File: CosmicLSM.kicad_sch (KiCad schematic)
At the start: 49 parts, among them J1 BAT, J2 JST GH, J3 USB_C_Receptacle_USB2.0, SW1 SW_SPDT, SW2 SW_SPST, U1 SMF05CT1G, U2 SMF05CT1G, U3 M3406, U4 IP2312, U5 LSM6DSV, U6 ESP32-C3-WROOM-02-N4

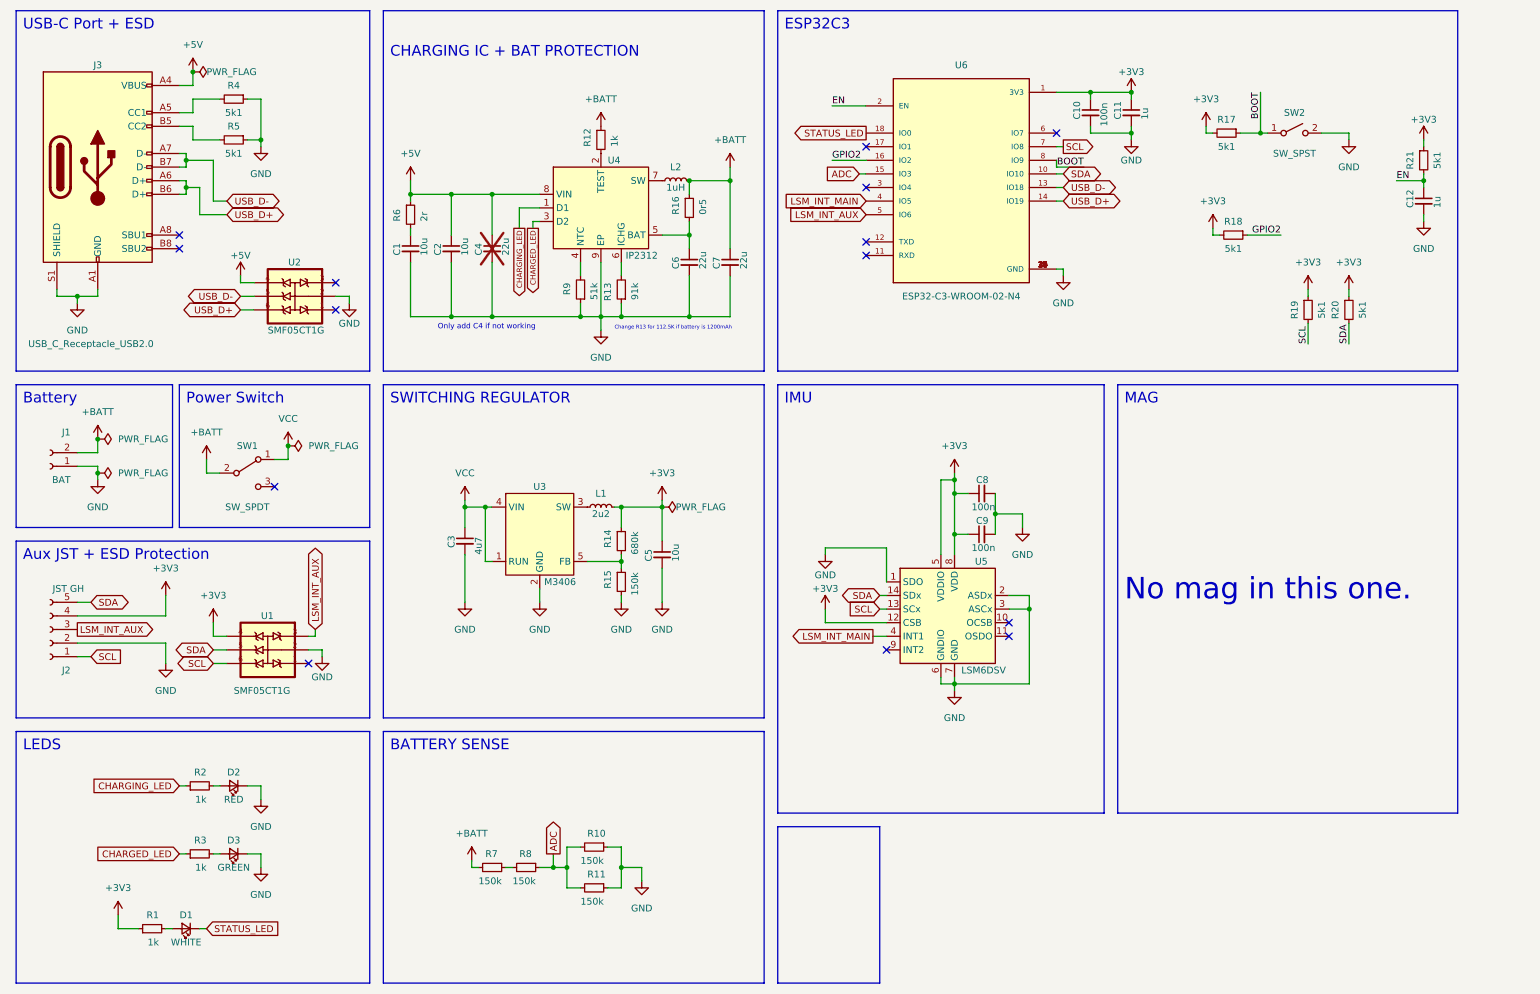
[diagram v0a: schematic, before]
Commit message: use ESP32-C6 in schematic
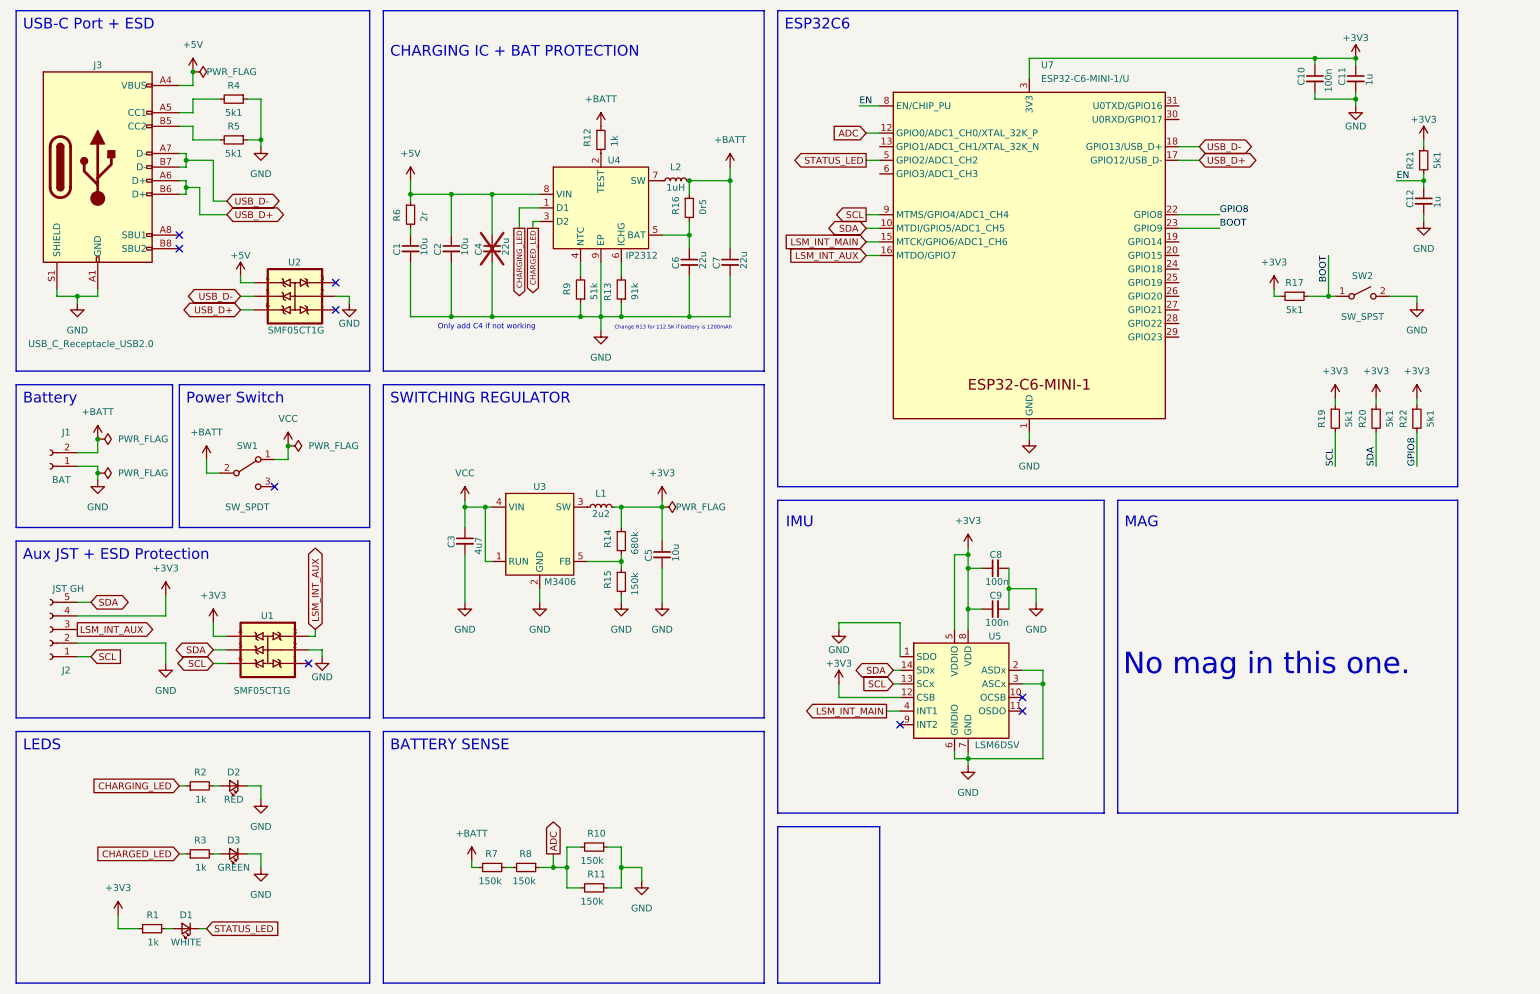
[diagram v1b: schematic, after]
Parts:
- removed R18: 5k1, Resistor_SMD:R_0603_1608Metric_Pad0.98x0.95mm_HandSolder, symbol CosmicLSM_Symbols:R_Small
- removed U6: ESP32-C3-WROOM-02-N4, footprints:MODULE_ESP32-C3-WROOM-02-H4, symbol CosmicLSM_Symbols:ESP32-C3-WROOM-02-N4
- added R22: 5k1, Resistor_SMD:R_0603_1608Metric_Pad0.98x0.95mm_HandSolder, symbol CosmicLSM_Symbols:R_Small
- added U7: ESP32-C6-MINI-1/U, Espressif:ESP32-C6-MINI-1, symbol Espressif:ESP32-C6-MINI-1/U
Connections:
- net +3V3: now also R22.1, U7.3 (3V3)
- net ADC: now also U7.12 (GPIO0/ADC1_CH0/XTAL_32K_P)
- net BOOT: now also U7.23 (GPIO9)
- net EN: now also U7.8 (EN/CHIP_PU)
- net GND: now also U7.1 (GND), U7.11 (GND), U7.14 (GND), U7.2 (GND), U7.36 (GND), U7.37 (GND), U7.38 (GND), U7.39 (GND), U7.40 (GND), U7.41 (GND), U7.42 (GND), U7.43 (GND), U7.44 (GND), U7.45 (GND), U7.46 (GND), U7.47 (GND), U7.48 (GND), U7.49 (GND), U7.50 (GND), U7.51 (GND), U7.52 (GND), U7.53 (GND)
- net LSM_INT_AUX: now also U7.16 (MTDO/GPIO7)
- net LSM_INT_MAIN: now also U7.15 (MTCK/GPIO6/ADC1_CH6)
- net SCL: now also U7.9 (MTMS/GPIO4/ADC1_CH4)
- net SDA: now also U7.10 (MTDI/GPIO5/ADC1_CH5)
- net STATUS_LED: now also U7.5 (GPIO2/ADC1_CH2)
- net USB_D+: now also U7.17 (GPIO12/USB_D-)
- net USB_D-: now also U7.18 (GPIO13/USB_D+)
- new net GPIO8: R22.2, U7.22 (GPIO8)
- no-connect marks 14 -> 9
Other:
- note added: "ESP32C6"
- note removed: "ESP32C3"
- moved on the sheet: C8, C9, R17, R19, R20, SW2, U5

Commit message: new data
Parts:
- U5: value LSM6DSV -> BMI160
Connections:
- net LSM_INT_MAIN: now also U7.26 (GPIO20); no longer U7.15 (MTCK/GPIO6/ADC1_CH6)
- net SCL: now also U7.28 (GPIO22); no longer U7.9 (MTMS/GPIO4/ADC1_CH4)
- net SDA: now also U7.27 (GPIO21); no longer U7.10 (MTDI/GPIO5/ADC1_CH5)
- net USB_D+: now also U2.5; no longer U2.6
- net USB_D-: now also U2.6; no longer U2.5
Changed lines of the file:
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@@
 	(wire
 		(pts
-			(xy 172.72 54.61) (xy 175.26 54.61)
-		)
-		(stroke
-			(width 0)
-			(type default)
-		)
-	)
-	(wire
-		(pts
 			(xy 73.66 67.31) (xy 76.2 67.31)
 		)
@@
 	(wire
 		(pts
-			(xy 45.72 41.91) (xy 45.72 40.64)
+			(xy 231.14 67.31) (xy 236.22 67.31)
 		)
 		(stroke
@@
 	(wire
 		(pts
-			(xy 172.72 57.15) (xy 175.26 57.15)
+			(xy 231.14 72.39) (xy 236.22 72.39)
+		)
+		(stroke
+			(width 0)
+			(type default)
+		)
+	)
+	(wire
+		(pts
+			(xy 45.72 41.91) (xy 45.72 40.64)
 		)
 		(stroke
@@
 	(wire
 		(pts
-			(xy 172.72 52.07) (xy 175.26 52.07)
-		)
-		(stroke
-			(width 0)
-			(type default)
-		)
-	)
-	(wire
-		(pts
 			(xy 116.84 173.99) (xy 116.84 170.18)
 		)
@@
 	(wire
 		(pts
+			(xy 231.14 69.85) (xy 236.22 69.85)
+		)
+		(stroke
+			(width 0)
+			(type default)
+		)
+	)
+	(wire
+		(pts
 			(xy 124.46 170.18) (xy 127 170.18)
 		)
@@
 		)
 	)
-	(global_label "USB_D-"
+	(global_label "USB_D+"
 		(shape bidirectional)
 		(at 55.88 67.31 180)
@@
 		)
 	)
-	(global_label "USB_D+"
+	(global_label "USB_D-"
 		(shape bidirectional)
 		(at 55.88 69.85 180)
@@
 	(global_label "SDA"
 		(shape bidirectional)
-		(at 172.72 54.61 180)
+		(at 236.22 69.85 0)
 		(fields_autoplaced yes)
 		(effects
@@
 				(size 1.27 1.27)
 			)
-			(justify right)
+			(justify left)
 		)
 		(property "Intersheetrefs" "${INTERSHEET_REFS}"
-			(at 165.0554 54.61 0)
+			(at 243.8846 69.85 0)
 			(effects
 				(font
 					(size 1.27 1.27)
 				)
-				(justify right)
+				(justify left)
 				(hide yes)
 			)
@@
 	(global_label "LSM_INT_MAIN"
 		(shape input)
-		(at 172.72 57.15 180)
+		(at 236.22 67.31 0)
 		(fields_autoplaced yes)
 		(effects
@@
 				(size 1.27 1.27)
 			)
-			(justify right)
+			(justify left)
 		)
 		(property "Intersheetrefs" "${INTERSHEET_REFS}"
-			(at 156.7324 57.15 0)
+			(at 252.2076 67.31 0)
 			(effects
 				(font
 					(size 1.27 1.27)
 				)
-				(justify right)
+				(justify left)
 				(hide yes)
 			)
@@
 	(global_label "SCL"
 		(shape output)
-		(at 172.72 52.07 180)
+		(at 236.22 72.39 0)
 		(fields_autoplaced yes)
 		(effects
@@
 				(size 1.27 1.27)
 			)
-			(justify right)
+			(justify left)
 		)
 		(property "Intersheetrefs" "${INTERSHEET_REFS}"
-			(at 166.2272 52.07 0)
+			(at 242.7128 72.39 0)
 			(effects
 				(font
 					(size 1.27 1.27)
 				)
-				(justify right)
+				(justify left)
 				(hide yes)
 			)
@@
 			)
 		)
-		(property "Value" "LSM6DSV"
+		(property "Value" "BMI160"
 			(at 193.04 151.13 0)
 			(effects

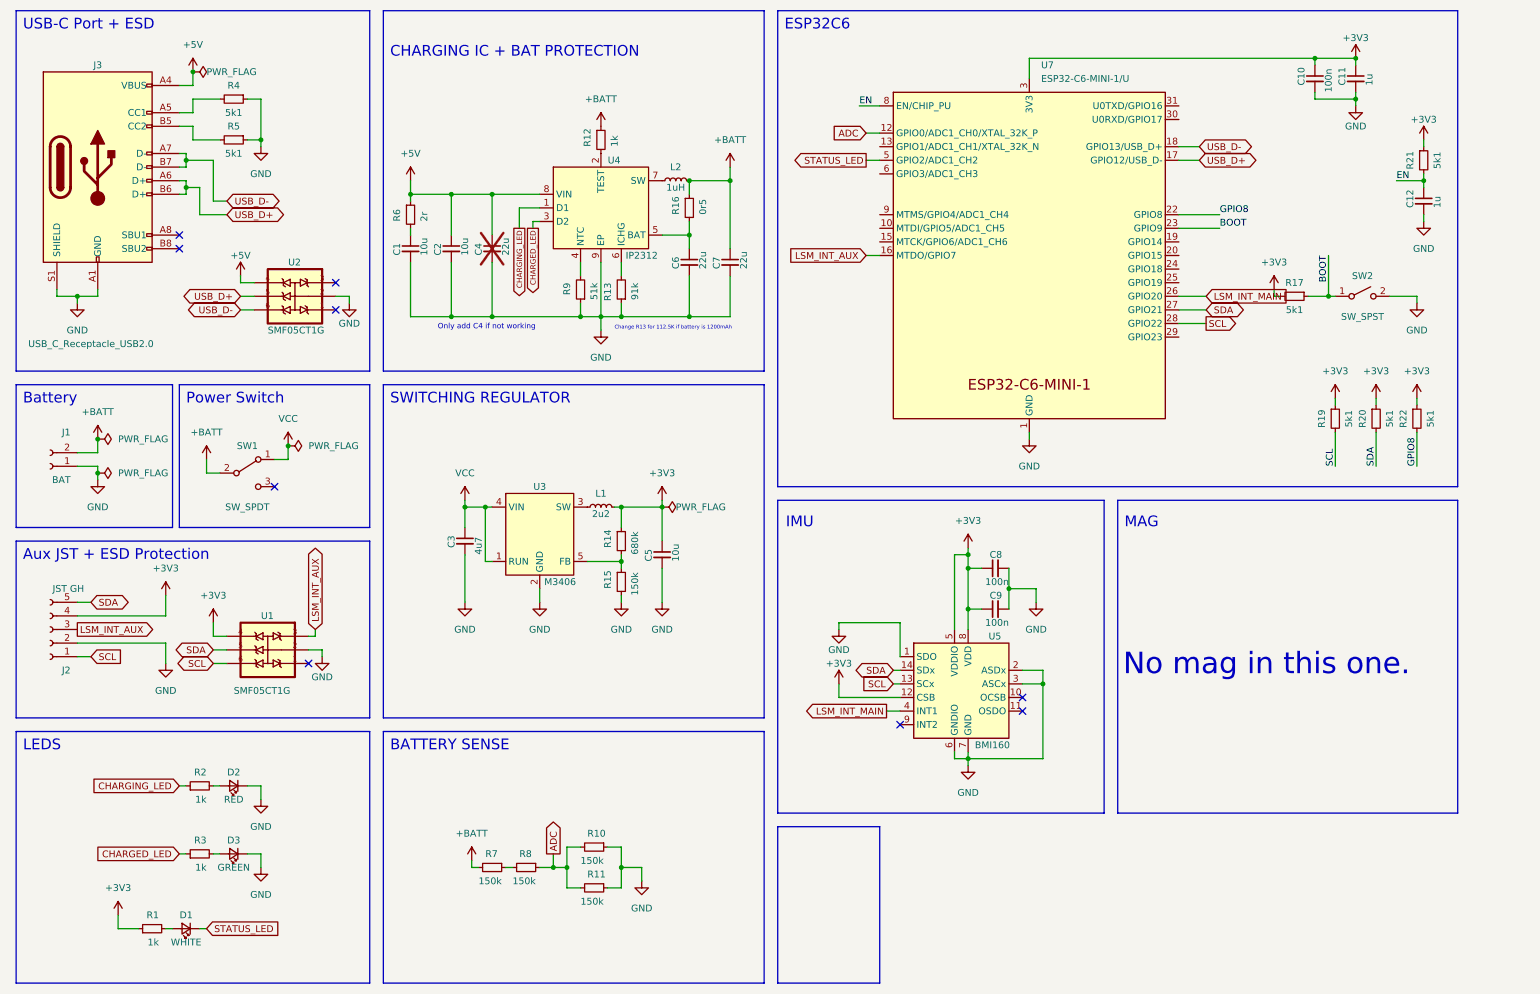
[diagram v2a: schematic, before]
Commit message: remove backup files
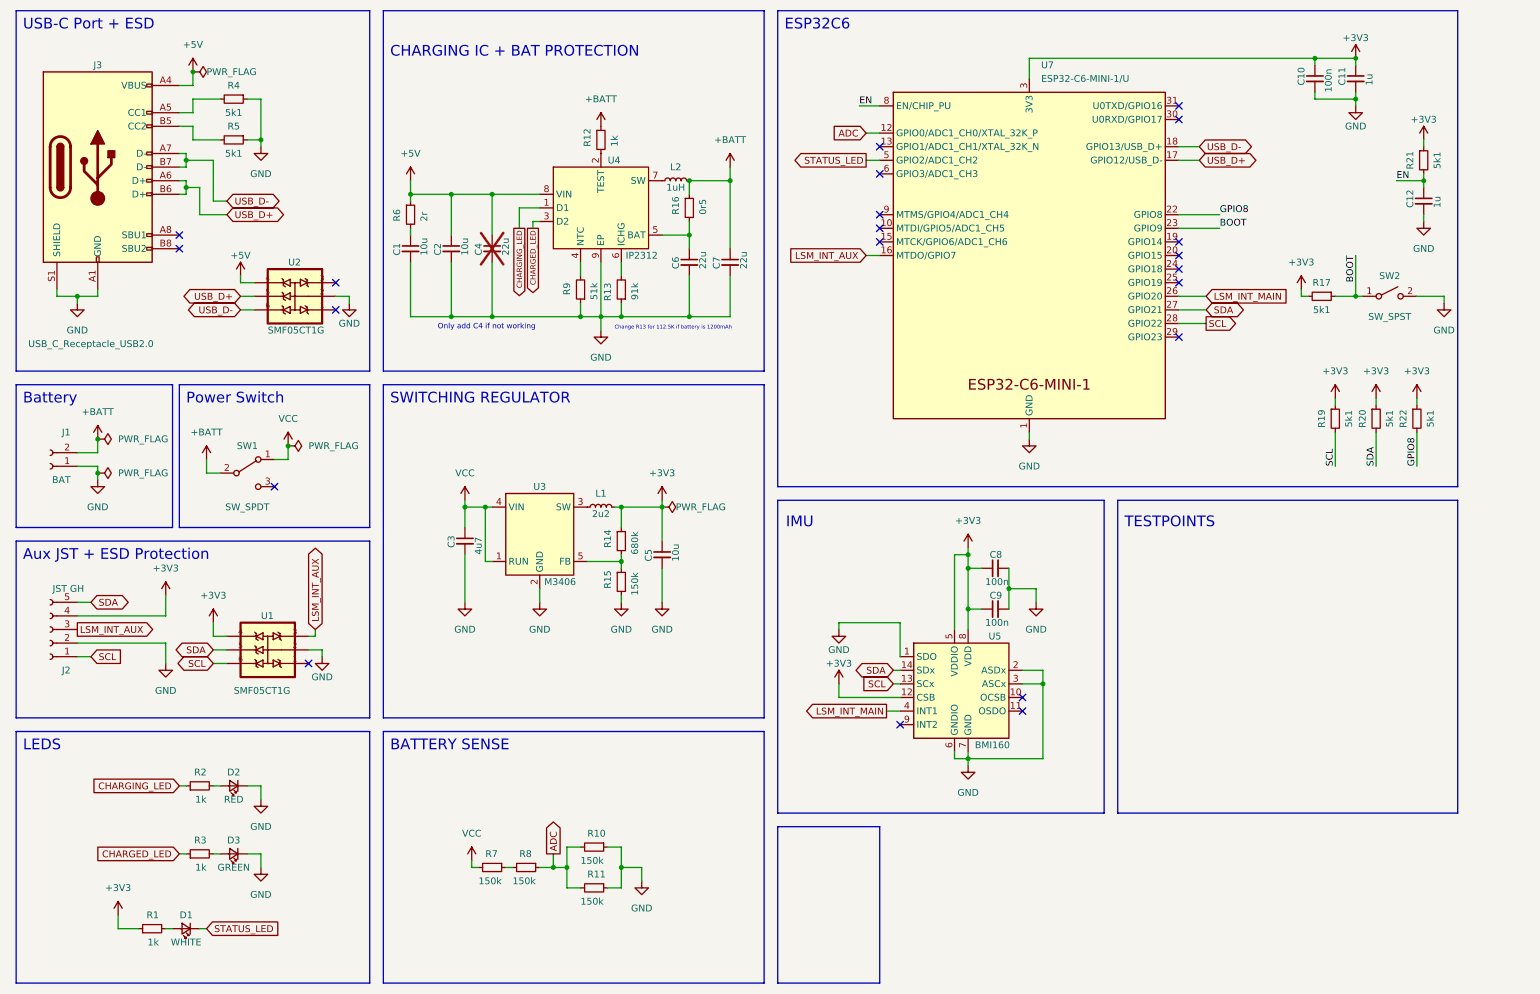
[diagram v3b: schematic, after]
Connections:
- net +BATT: no longer R7.2
- net VCC: now also R7.2
- no-connect marks 9 -> 21
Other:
- note added: "TESTPOINTS"
- note removed: "MAG"
- note removed: "No mag in this one."
- company: KOUNOLAB -> (none)
- title: CosmicLSM -> Waifutracker
- moved on the sheet: R17, SW2
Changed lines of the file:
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@@
 	(paper "A4")
 	(title_block
-		(title "CosmicLSM")
-		(date "2023-09-07")
-		(rev "v1.0")
-		(company "KOUNOLAB")
+		(title "Waifutracker")
+		(date "2024-05-08")
+		(rev "v0.1")
 		(comment 1 "Currently untested!")
 		(comment 2 "Licensed under CERN-OHL-P 2")
-		(comment 3 "especially Gorbit99 and wigwagwent <3")
-		(comment 4 "Thanks to everyone in the SlimeVR DIY community,")
+		(comment 3 "Thanks to everyone in the SlimeVR DIY community,")
 	)
 	(junction
@@
 	)
 	(junction
-		(at 259.08 67.31)
+		(at 264.16 67.31)
 		(diameter 0)
 		(color 0 0 0 0)
@@
 	)
 	(no_connect
+		(at 231.14 62.23)
+	)
+	(no_connect
+		(at 175.26 54.61)
+	)
+	(no_connect
+		(at 231.14 34.29)
+	)
+	(no_connect
+		(at 175.26 52.07)
+	)
+	(no_connect
+		(at 231.14 64.77)
+	)
+	(no_connect
+		(at 231.14 74.93)
+	)
+	(no_connect
+		(at 175.26 44.45)
+	)
+	(no_connect
 		(at 62.23 102.87)
 	)
@@
 	)
 	(no_connect
+		(at 231.14 59.69)
+	)
+	(no_connect
 		(at 73.66 69.85)
 	)
 	(no_connect
+		(at 175.26 39.37)
+	)
+	(no_connect
+		(at 231.14 31.75)
+	)
+	(no_connect
+		(at 175.26 57.15)
+	)
+	(no_connect
 		(at 73.66 64.77)
 	)
+	(no_connect
+		(at 231.14 57.15)
+	)
 	(wire
 		(pts
@@
 	(wire
 		(pts
-			(xy 248.92 66.04) (xy 248.92 67.31)
+			(xy 254 66.04) (xy 254 67.31)
 		)
 		(stroke
@@
 	(wire
 		(pts
-			(xy 259.08 67.31) (xy 260.35 67.31)
+			(xy 264.16 67.31) (xy 265.43 67.31)
 		)
 		(stroke
@@
 	(wire
 		(pts
-			(xy 270.51 67.31) (xy 275.59 67.31)
+			(xy 275.59 67.31) (xy 280.67 67.31)
 		)
 		(stroke
@@
 	(wire
 		(pts
-			(xy 255.27 67.31) (xy 259.08 67.31)
+			(xy 260.35 67.31) (xy 264.16 67.31)
 		)
 		(stroke
@@
 	(wire
 		(pts
-			(xy 250.19 67.31) (xy 248.92 67.31)
+			(xy 255.27 67.31) (xy 254 67.31)
 		)
 		(stroke
@@
 	(wire
 		(pts
-			(xy 275.59 67.31) (xy 275.59 68.58)
+			(xy 280.67 67.31) (xy 280.67 68.58)
 		)
 		(stroke
@@
 	(wire
 		(pts
-			(xy 259.08 59.69) (xy 259.08 67.31)
+			(xy 264.16 59.69) (xy 264.16 67.31)
 		)
 		(stroke
@@
 		)
 	)
-	(text "No mag in this one."
-		(exclude_from_sim no)
-		(at 220.726 138.43 0)
-		(effects
-			(font
-				(size 4 4)
-			)
-			(justify left bottom)
-		)
-	)
 	(text "ESP32C6\n"
 		(exclude_from_sim no)
@@
 		)
 	)
-	(text "MAG\n"
+	(text "TESTPOINTS"
 		(exclude_from_sim no)
 		(at 220.98 110.744 0)
@@
 	)
 	(label "BOOT"
-		(at 259.08 59.69 270)
+		(at 264.16 59.69 270)
 		(fields_autoplaced yes)
 		(effects
@@
 	(symbol
 		(lib_id "power:+3V3")
-		(at 248.92 66.04 0)
+		(at 254 66.04 0)
 		(unit 1)
 		(exclude_from_sim no)
@@
 		(fields_autoplaced yes)
 		(property "Reference" "#PWR037"
-			(at 248.92 69.85 0)
+			(at 254 69.85 0)
 			(effects
 				(font
@@
 		)
 		(property "Value" "+3V3"
-			(at 248.92 60.96 0)
+			(at 254 60.96 0)
 			(effects
 				(font
@@
 		)
 		(property "Footprint" ""
-			(at 248.92 66.04 0)
+			(at 254 66.04 0)
 			(effects
 				(font
@@
 		)
 		(property "Datasheet" ""
-			(at 248.92 66.04 0)
+			(at 254 66.04 0)
 			(effects
 				(font
@@
 		)
 		(property "Description" ""
-			(at 248.92 66.04 0)
+			(at 254 66.04 0)
 			(effects
 				(font
@@
 			)
 		)
-		(property "Value" "+BATT"
+		(property "Value" "VCC"
 			(at 99.06 167.64 0)
 			(effects
@@
 	(symbol
 		(lib_id "power:GND")
-		(at 275.59 68.58 0)
+		(at 280.67 68.58 0)
 		(unit 1)
 		(exclude_from_sim no)
@@
 		(fields_autoplaced yes)
 		(property "Reference" "#PWR039"
-			(at 275.59 74.93 0)
+			(at 280.67 74.93 0)
 			(effects
 				(font
@@
 		)
 		(property "Value" "GND"
-			(at 275.59 73.66 0)
+			(at 280.67 73.66 0)
 			(effects
 				(font
@@
 		)
 		(property "Footprint" ""
-			(at 275.59 68.58 0)
+			(at 280.67 68.58 0)
 			(effects
 				(font
@@
 		)
 		(property "Datasheet" ""
-			(at 275.59 68.58 0)
+			(at 280.67 68.58 0)
 			(effects
 				(font
@@
 		)
 		(property "Description" ""
-			(at 275.59 68.58 0)
+			(at 280.67 68.58 0)
 			(effects
 				(font
@@
 	(symbol
 		(lib_id "CosmicLSM_Symbols:SW_SPST")
-		(at 265.43 67.31 0)
+		(at 270.51 67.31 0)
 		(unit 1)
 		(exclude_from_sim no)
@@
 		(dnp no)
 		(property "Reference" "SW2"
-			(at 265.43 63.5 0)
+			(at 270.51 63.5 0)
 			(effects
 				(font
@@
 		)
 		(property "Value" "SW_SPST"
-			(at 265.43 71.12 0)
+			(at 270.51 71.12 0)
 			(effects
 				(font
@@
 		)
 		(property "Footprint" "Button_Switch_SMD:SW_SPST_B3U-1000P"
-			(at 265.43 67.31 0)
+			(at 270.51 67.31 0)
 			(effects
 				(font
@@
 		)
 		(property "Datasheet" "~"
-			(at 265.43 67.31 0)
+			(at 270.51 67.31 0)
 			(effects
 				(font
@@
 		)
 		(property "Description" ""
-			(at 265.43 67.31 0)
+			(at 270.51 67.31 0)
 			(effects
 				(font
@@
 	(symbol
 		(lib_id "CosmicLSM_Symbols:R_Small")
-		(at 252.73 67.31 270)
+		(at 257.81 67.31 270)
 		(unit 1)
 		(exclude_from_sim no)
@@
 		(dnp no)
 		(property "Reference" "R17"
-			(at 252.73 64.77 90)
+			(at 257.81 64.77 90)
 			(effects
 				(font
@@
 		)
 		(property "Value" "5k1"
-			(at 252.73 69.85 90)
+			(at 257.81 69.85 90)
 			(effects
 				(font
@@
 		)
 		(property "Footprint" "Resistor_SMD:R_0603_1608Metric_Pad0.98x0.95mm_HandSolder"
-			(at 252.73 67.31 0)
+			(at 257.81 67.31 0)
 			(effects
 				(font
@@
 		)
 		(property "Datasheet" "~"
-			(at 252.73 67.31 0)
+			(at 257.81 67.31 0)
 			(effects
 				(font
@@
 		)
 		(property "Description" ""
-			(at 252.73 67.31 0)
+			(at 257.81 67.31 0)
 			(effects
 				(font
